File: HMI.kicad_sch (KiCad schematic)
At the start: 1 part, among them SW1 RotaryEncoder_Switch_4P

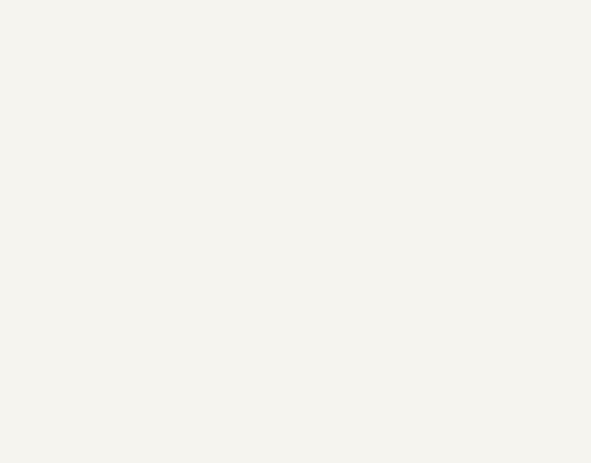
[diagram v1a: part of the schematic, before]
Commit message: added TFT Display
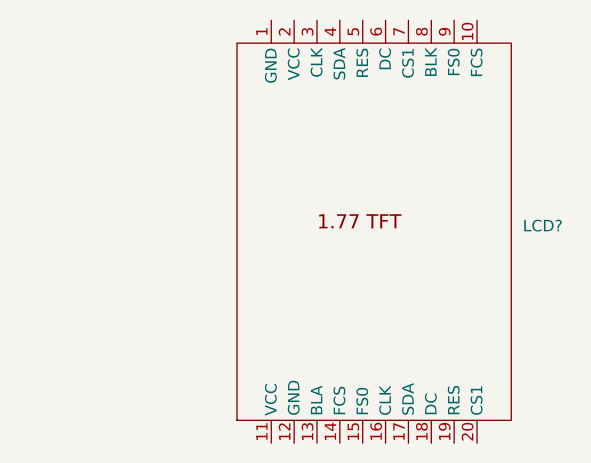
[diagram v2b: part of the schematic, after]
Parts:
- added LCD?: ~, Custom_Parts:HSB180S10B_TFT_Display, symbol Custom_Parts:HS180S10B_TFT_Display
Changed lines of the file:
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@@
 	(paper "A4")
+	(symbol
+		(lib_id "Custom_Parts:HS180S10B_TFT_Display")
+		(at 214.63 57.15 0)
+		(unit 1)
+		(exclude_from_sim no)
+		(in_bom yes)
+		(on_board yes)
+		(dnp no)
+		(fields_autoplaced yes)
+		(property "Reference" "LCD?"
+			(at 231.14 55.8799 0)
+			(effects
+				(font
+					(size 1.27 1.27)
+				)
+				(justify left)
+			)
+		)
+		(property "Value" "~"
+			(at 231.14 57.785 0)
+			(effects
+				(font
+					(size 1.27 1.27)
+				)
+				(justify left)
+			)
+		)
+		(property "Footprint" "Custom_Parts:HSB180S10B_TFT_Display"
+			(at 214.63 57.15 0)
+			(effects
+				(font
+					(size 1.27 1.27)
+				)
+				(hide yes)
+			)
+		)
+		(property "Datasheet" "https://atta.szlcsc.com/upload/public/pdf/source/20240813/B2A9CB96037A2CFF5EDEA82031799016.pdf"
+			(at 214.63 57.15 0)
+			(effects
+				(font
+					(size 1.27 1.27)
+				)
+				(hide yes)
+			)
+		)
+		(property "Description" "Main Control Chip:ST7735 Size:1.77 Pixel Resolution:160x128 Operating Temperature:-20°C~+70°C Operating Temperature:-20°C~+70°C"
+			(at 214.63 57.15 0)
+			(effects
+				(font
+					(size 1.27 1.27)
+				)
+				(hide yes)
+			)
+		)
+		(property "Manufacturer Part" "HS180S10B"
+			(at 214.63 57.15 0)
+			(effects
+				(font
+					(size 1.27 1.27)
+				)
+				(hide yes)
+			)
+		)
+		(property "Manufacturer" "HS(汉昇)"
+			(at 214.63 57.15 0)
+			(effects
+				(font
+					(size 1.27 1.27)
+				)
+				(hide yes)
+			)
+		)
+		(property "Supplier Part" "C5329585"
+			(at 214.63 57.15 0)
+			(effects
+				(font
+					(size 1.27 1.27)
+				)
+				(hide yes)
+			)
+		)
+		(property "Supplier" "LCSC"
+			(at 214.63 57.15 0)
+			(effects
+				(font
+					(size 1.27 1.27)
+				)
+				(hide yes)
+			)
+		)
+		(property "LCSC Part Name" "1.8寸128*160(RGB)彩色SPI串口TFT液晶显示屏"
+			(at 214.63 57.15 0)
+			(effects
+				(font
+					(size 1.27 1.27)
+				)
+				(hide yes)
+			)
+		)
+		(property "LSCS" "C5329585"
+			(at 214.63 57.15 0)
+			(effects
+				(font
+					(size 1.27 1.27)
+				)
+				(hide yes)
+			)
+		)
+		(pin "10"
+		)
+		(pin "14"
+		)
+		(pin "4"
+		)
+		(pin "1"
+		)
+		(pin "13"
+		)
+		(pin "5"
+		)
+		(pin "17"
+		)
+		(pin "2"
+		)
+		(pin "19"
+		)
+		(pin "12"
+		)
+		(pin "20"
+		)
+		(pin "8"
+		)
+		(pin "3"
+		)
+		(pin "18"
+		)
+		(pin "9"
+		)
+		(pin "15"
+		)
+		(pin "16"
+		)
+		(pin "11"
+		)
+		(pin "7"
+		)
+		(pin "6"
+		)
+		(instances
+			(project ""
+				(path "/ee47f507-02e8-4ef5-a6d4-1ac4b2022b93/1ab1902b-acf7-4c4c-8c09-61d5cb12072a"
+					(reference "LCD?")
+					(unit 1)
+				)
+			)
+		)
+	)
 	(symbol
 		(lib_id "Custom_Parts:RotaryEncoder_Switch_4P")

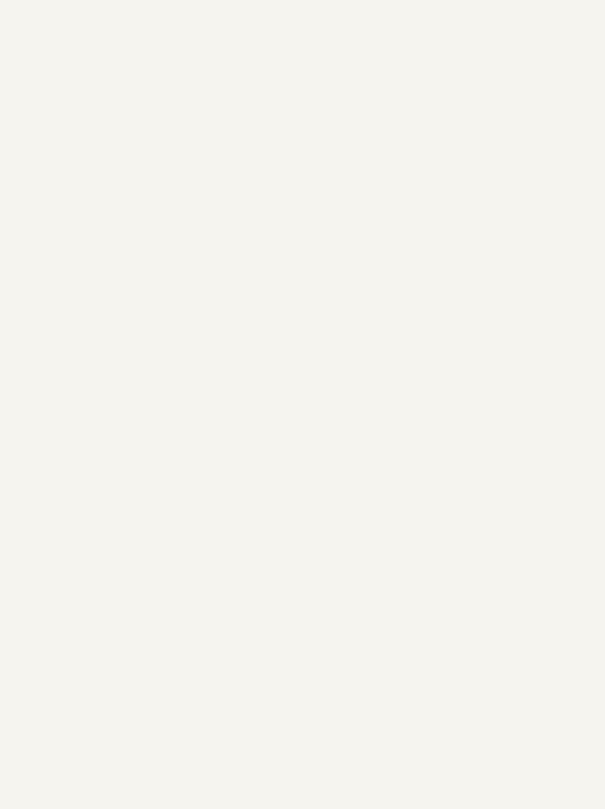
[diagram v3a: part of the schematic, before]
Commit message: added switches
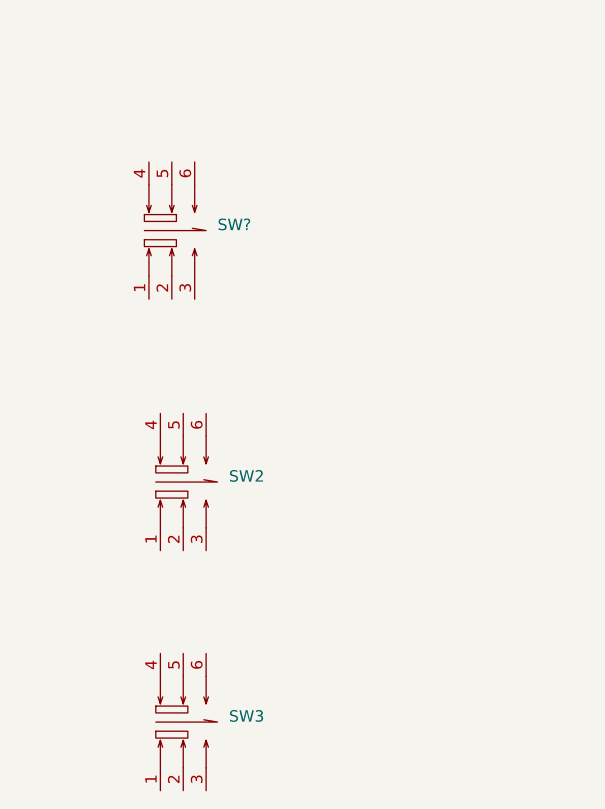
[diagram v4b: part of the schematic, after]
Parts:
- added SW2, SW3, SW?: ~, Custom_Parts:Switch_XKB5858, symbol Custom_Parts:Switch_XKB5858
